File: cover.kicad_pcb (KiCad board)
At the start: 2 copper layers, 102 x 81.5 mm, 4 parts

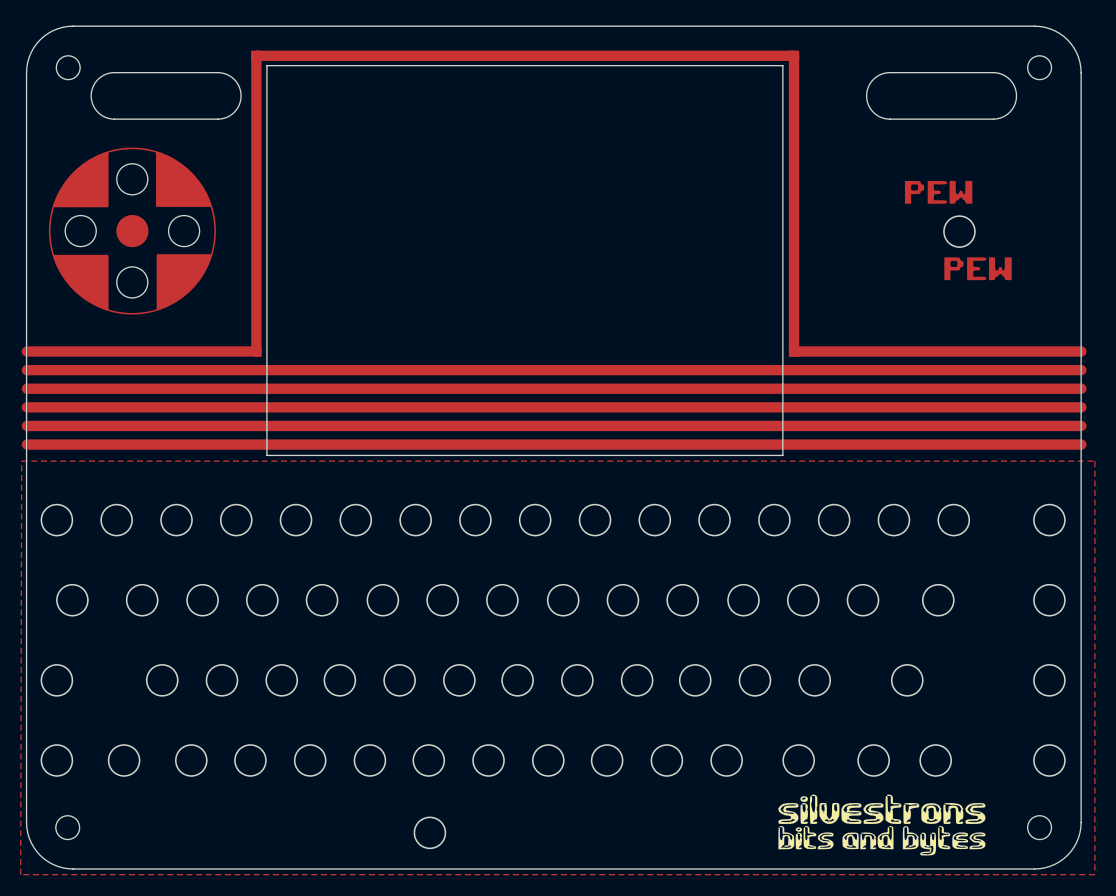
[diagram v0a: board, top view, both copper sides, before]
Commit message: updated top cover
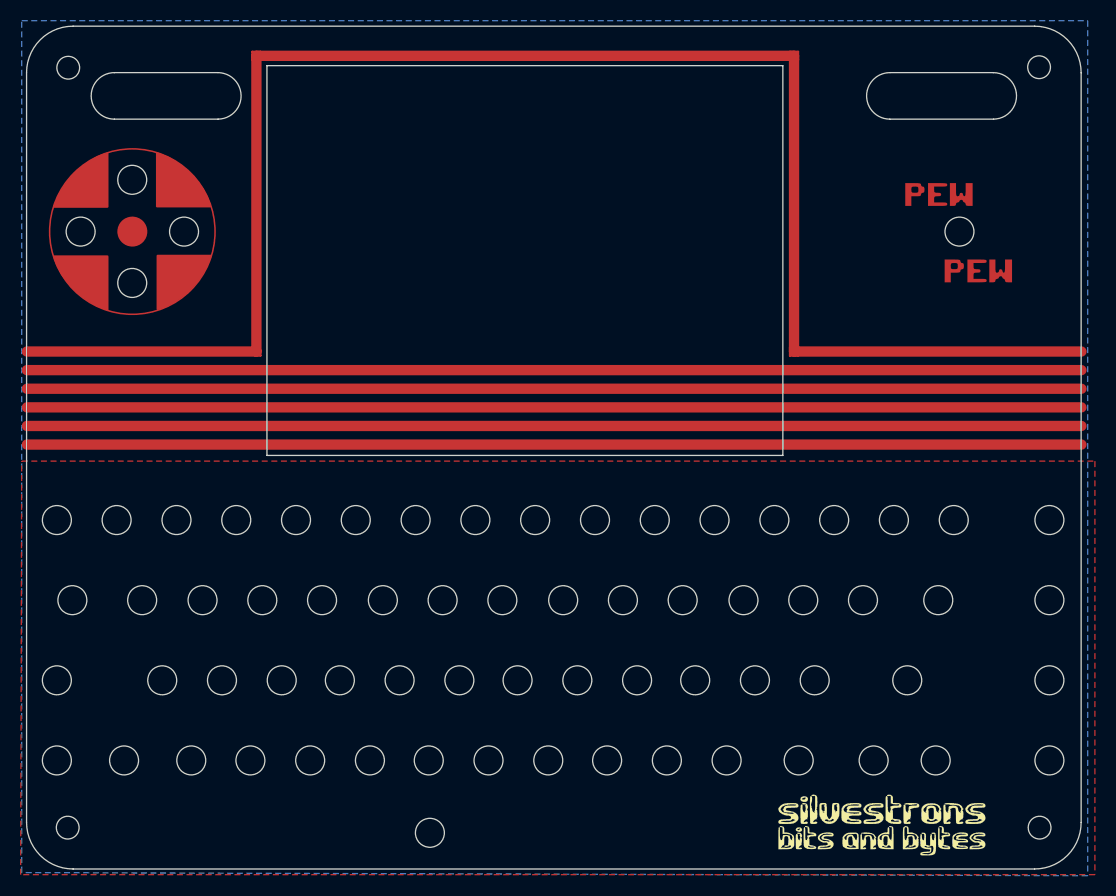
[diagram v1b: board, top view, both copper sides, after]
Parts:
- removed the G*** at (189.6, 99.0) (x2)
- removed the G*** at (190.7, 100.0)
- added REF**: 64-mini-pewpew, Silvestron Components:64-mini-pewpew, F.Cu at (230.0, 79.3)
- added REF**: MountingHole_2.2mm_M2_NoPad, Silvestron Components:MountingHole_2.2mm_M2_NoPad, F.Cu at (237.7, 63.4)
- added REF**: 64-mini-dpad, Silvestron Components:64-mini-dpad, F.Cu at (150.0, 79.3)
- added REF**: 64-mini-keyboard, Silvestron Components:64-mini-keyboard, F.Cu at (190.8, 100.2)
- added REF**: MountingHole_2.2mm_M2_NoPad, Silvestron Components:MountingHole_2.2mm_M2_NoPad, F.Cu at (237.8, 136.9)
- added REF**: MountingHole_2.2mm_M2_NoPad, Silvestron Components:MountingHole_2.2mm_M2_NoPad, F.Cu at (143.8, 63.5)
- added REF**: MountingHole_2.2mm_M2_NoPad, Silvestron Components:MountingHole_2.2mm_M2_NoPad, F.Cu at (143.8, 136.9)
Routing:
- added copper zone on B.Cu, net (none)
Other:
- outline, holes or cut-outs redrawn
- board text added: "JLCJLCJLCJLC"
